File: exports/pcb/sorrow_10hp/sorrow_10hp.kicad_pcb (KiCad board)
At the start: 2 copper layers, 50.8 x 128.5 mm, 1 part

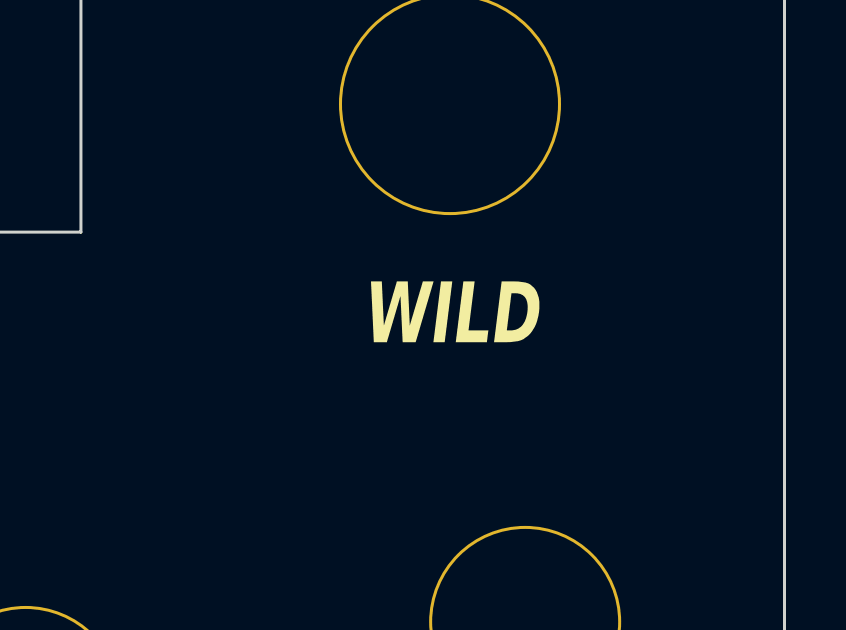
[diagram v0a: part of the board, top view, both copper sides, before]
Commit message: Sorrow: WILDNESS in full, and the preview stops lying about centring
There is room, so the Kit-page label is WILDNESS rather than WILD.

David spotted the italic labels sitting left of their holes. The board was always
right - the emitted gr_text has no justify, so KiCad centres it, and the file has
"WILDNESS" at exactly 39.649996 against a pot at 39.650. It was the preview.

Shearing a scratch layer moves the ink sideways, and I was centring the tile
rather than the ink that survived the shear, so italics landed ~0.9 mm left. Now
the tile is placed by the sheared ink's own bounding box. Measured off the
rendered PNG: every label within 0.05 mm of its hole, italic and upright alike,
where the italics were 0.88 to 0.95 mm out before.

Worth keeping: a preview that is drawn from the same tables as the gerbers can
still be wrong about the gerbers, if the drawing code adds something the board
does not have.

Co-Authored-By: Claude Opus 5 (1M context) <noreply@anthropic.com>
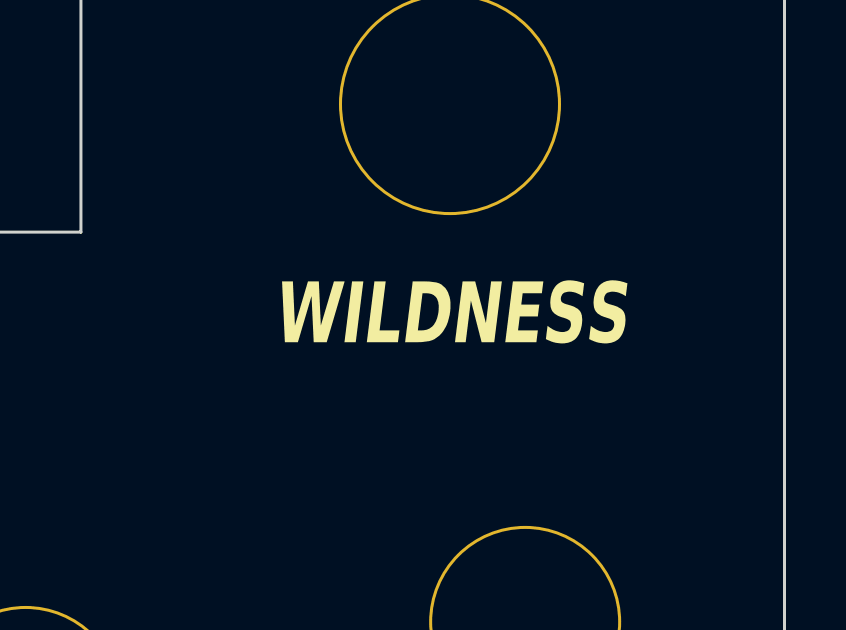
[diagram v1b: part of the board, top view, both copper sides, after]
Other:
- board text added: "WILDNESS"
- board text removed: "WILD"
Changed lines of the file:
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@@
 		(effects (font (size 2.6 1.872) (thickness 0.442) bold))
 	)
-	(gr_text "WILD" (at 39.649996 49.027311) (layer "F.SilkS")
+	(gr_text "WILDNESS" (at 39.649996 49.027311) (layer "F.SilkS")
 		(effects (font (size 2.028 1.4602) (thickness 0.345) bold italic))
 	)

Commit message: Sorrow: generated without the JLC marker, for the "remove order number" route
JLCPCB have a newer option that removes the order number outright, and David
confirms it worked on the Joy order. That changes which gerbers are right.

The JLCJLCJLCJLC marker is drawn geometry, not an instruction - 4.7 KB of stroke
lines in the back-silkscreen gerber. It only does anything if JLCPCB recognise it
and substitute the number. If "remove order number" means "do not add one", the
literal string prints on the back of the board instead.

So the two routes need different gerbers, and the README now says so. Sorrow is
generated with --no-jlc-marker, which drops its back silkscreen from 4.7 KB to
455 bytes of header.

Left open in the README: the Joy board was ordered with the marker present and
the number removed. Whether its back is blank or reads JLCJLCJLCJLC settles
whether any of this matters.

Co-Authored-By: Claude Opus 5 (1M context) <noreply@anthropic.com>
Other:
- board text removed: "JLCJLCJLCJLC"
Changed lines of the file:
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@@
 		(effects (font (size 3 2.16) (thickness 0.51) bold))
-	)
-	(gr_text "JLCJLCJLCJLC" (at 25.4 75) (layer "B.SilkS")
-		(effects (font (size 1 1) (thickness 0.15)) (justify mirror))
 	)
 	(footprint "faceplate:holes" (layer "F.Cu")
